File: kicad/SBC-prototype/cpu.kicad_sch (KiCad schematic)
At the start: 5 parts, among them IC2 W65C02S6TPG-14

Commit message: Started including hierarchical flow in the top level sheet
- First, hierarchical designs - I don't need a schematic to all fit on
  one sheet.
- I had the clock and reset lines as global labels, so I converted them
  to hierarchical labels instead, imported them on each sheet, and then
  connected the sheets together. It probably looks like overkill right
  now, but it will allow me to modify each block more easily
- The VIA has unconnected ports for now because I haven't wired them to
  anything on the prototyep in the lab yet. That's next, once the
  EEPROM, SRAM, and address decoders are all working (and VIA1 doesn't
  need a load except for maybe some resistors for now).
- Finally, the power rails and ground are global labels right now and
  aren't connected to anything on the top level design schematic. I'm
  not sure if that's normal, so for now I've just left them.
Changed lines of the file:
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@@
 	(title_block
 		(title "65C02 Single Board Computer")
-		(rev "Mk. 0")
+		(rev "Proto")
 	)
 	(junction
@@
 			(width 0)
 			(type default)
-		)
-	)
-	(global_label "~{RST}"
-		(shape input)
-		(at 54.61 60.96 180)
-		(fields_autoplaced yes)
-		(effects
-			(font
-				(size 1.27 1.27)
-			)
-			(justify right)
-		)
-		(property "Intersheetrefs" "${INTERSHEET_REFS}"
-			(at 48.1777 60.96 0)
-			(effects
-				(font
-					(size 1.27 1.27)
-				)
-				(justify right)
-				(hide yes)
-			)
-		)
-	)
-	(global_label "CLK"
-		(shape input)
-		(at 54.61 85.09 180)
-		(fields_autoplaced yes)
-		(effects
-			(font
-				(size 1.27 1.27)
-			)
-			(justify right)
-		)
-		(property "Intersheetrefs" "${INTERSHEET_REFS}"
-			(at 48.0567 85.09 0)
-			(effects
-				(font
-					(size 1.27 1.27)
-				)
-				(justify right)
-				(hide yes)
-			)
 		)
 	)
@@
 		)
 	)
+	(hierarchical_label "CLK"
+		(shape input)
+		(at 54.61 85.09 180)
+		(fields_autoplaced yes)
+		(effects
+			(font
+				(size 1.27 1.27)
+			)
+			(justify right)
+		)
+	)
 	(hierarchical_label "DATA"
 		(shape bidirectional)
@@
 		)
 	)
+	(hierarchical_label "~{RST}"
+		(shape input)
+		(at 54.61 60.96 180)
+		(fields_autoplaced yes)
+		(effects
+			(font
+				(size 1.27 1.27)
+			)
+			(justify right)
+		)
+	)

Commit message: The pull up resistor for the IRQB and NMIB lines should be 3.3k ohms.
- This might not be accurate - depends on if my interrupt source (the
  65C22) is a n 'S' variant or not, which can pull both up and down.
- That's going to be an inportant detail when it comes to adding other
  VIA because if it pulls both ways, I'll need to AND the interrupt
  sources together instead of wired-OR'ing them.
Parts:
- R3, R4: value 1k -> 3k3
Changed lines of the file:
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@@
 			)
 		)
-		(property "Value" "1k"
+		(property "Value" "3k3"
 			(at 109.22 50.7999 0)
 			(effects
@@
 			)
 		)
-		(property "Value" "1k"
+		(property "Value" "3k3"
 			(at 118.11 50.7999 0)
 			(effects

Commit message: Removed pull up resistor on the IRQB line from VIA 1 to the processor. Confirmed 65C22S with totem pole IRQ.
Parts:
- removed R4: 3k3, symbol Device:R
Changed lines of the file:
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@@
-	)
-	(junction
-		(at 106.68 38.1)
-		(diameter 0)
-		(color 0 0 0 0)
-	)
-	(junction
-		(at 115.57 93.98)
-		(diameter 0)
-		(color 0 0 0 0)
 	)
 	(junction
@@
 	(wire
 		(pts
-			(xy 115.57 93.98) (xy 133.35 93.98)
+			(xy 54.61 93.98) (xy 133.35 93.98)
 		)
 		(stroke
@@
 		)
 	)
-	(wire
-		(pts
-			(xy 54.61 93.98) (xy 115.57 93.98)
-		)
-		(stroke
-			(width 0)
-			(type default)
-		)
-	)
 	(bus
 		(pts
@@
 		)
 	)
-	(wire
-		(pts
-			(xy 115.57 53.34) (xy 115.57 93.98)
-		)
-		(stroke
-			(width 0)
-			(type default)
-		)
-	)
 	(bus
 		(pts
@@
 		)
 	)
-	(wire
-		(pts
-			(xy 115.57 38.1) (xy 115.57 45.72)
-		)
-		(stroke
-			(width 0)
-			(type default)
-		)
-	)
 	(bus
 		(pts
@@
 		(pts
 			(xy 196.85 73.66) (xy 196.85 76.2)
-		)
-		(stroke
-			(width 0)
-			(type default)
-		)
-	)
-	(wire
-		(pts
-			(xy 106.68 38.1) (xy 115.57 38.1)
 		)
 		(stroke
@@
 					(unit 1)
 				)
-			)
-		)
-	)
-	(symbol
-		(lib_id "Device:R")
-		(at 115.57 49.53 0)
-		(unit 1)
-		(exclude_from_sim no)
-		(in_bom yes)
-		(on_board yes)
-		(dnp no)
-		(fields_autoplaced yes)
-		(property "Reference" "R4"
-			(at 118.11 48.2599 0)
-			(effects
-				(font
-					(size 1.27 1.27)
-				)
-				(justify left)
-			)
-		)
-		(property "Value" "3k3"
-			(at 118.11 50.7999 0)
-			(effects
-				(font
-					(size 1.27 1.27)
-				)
-				(justify left)
-			)
-		)
-		(property "Footprint" ""
-			(at 113.792 49.53 90)
-			(effects
-				(font
-					(size 1.27 1.27)
-				)
-				(hide yes)
-			)
-		)
-		(property "Datasheet" "~"
-			(at 115.57 49.53 0)
-			(effects
-				(font
-					(size 1.27 1.27)
-				)
-				(hide yes)
-			)
-		)
-		(property "Description" "Resistor"
-			(at 115.57 49.53 0)
-			(effects
-				(font
-					(size 1.27 1.27)
-				)
-				(hide yes)
-			)
-		)
-		(pin "1"
-		)
-		(pin "2"
-		)
-		(instances
-			(project "SBC-prototype"
-				(path "/1c8fb460-190a-4823-a6aa-9b1d397d6158/0456201c-b4b8-4a85-8590-2dcf9ac729a4"
-					(reference "R4")
-					(unit 1)
-				)

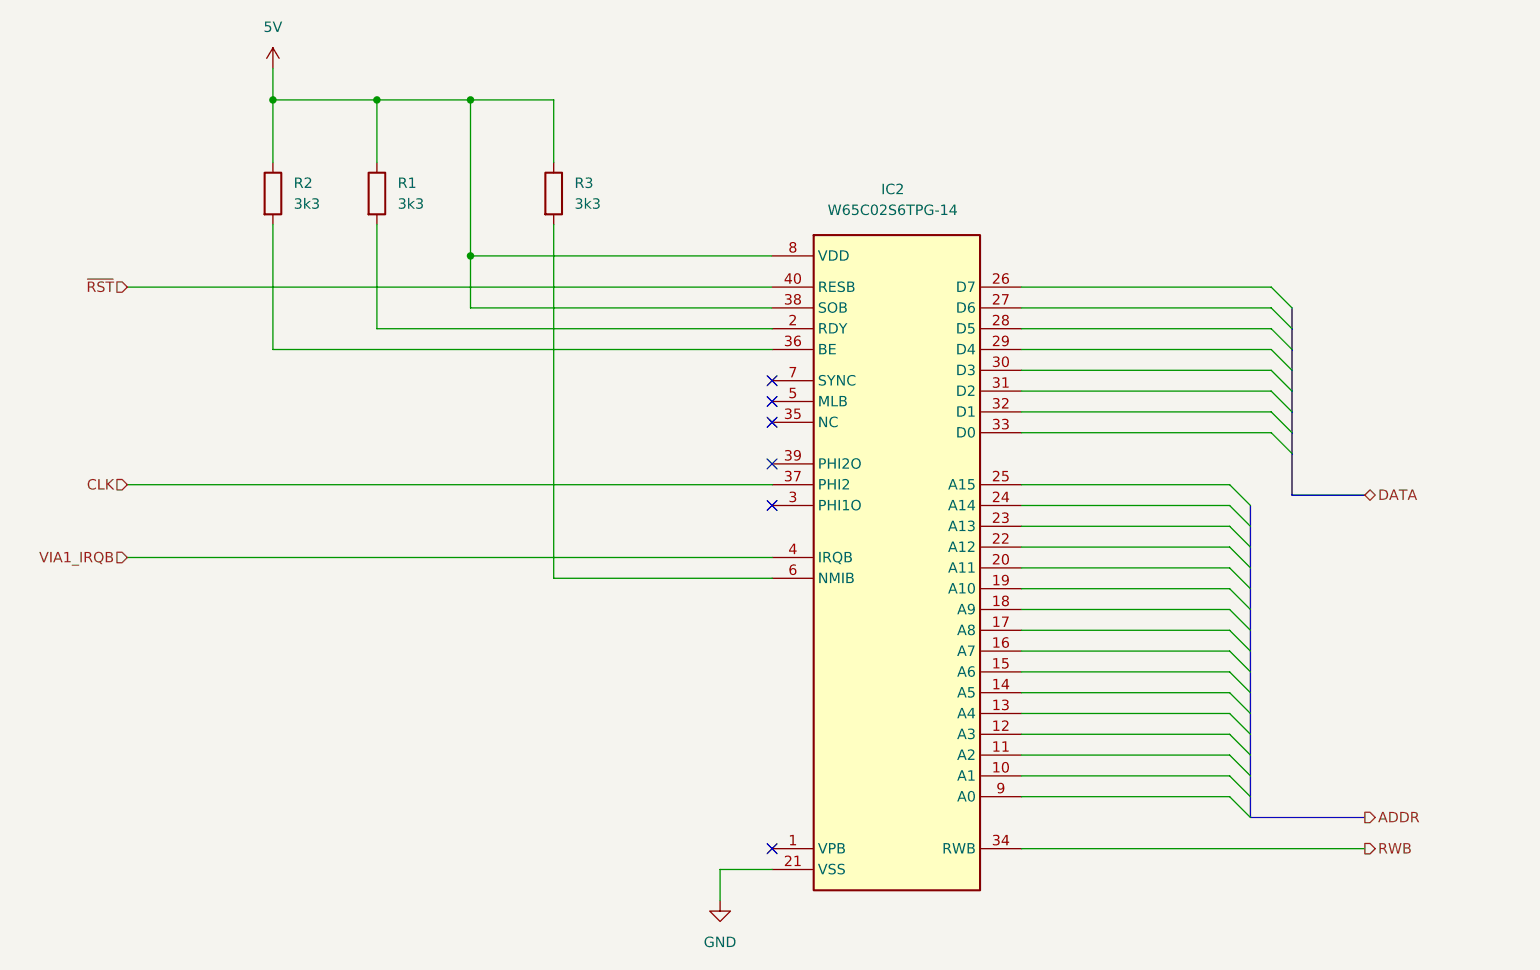
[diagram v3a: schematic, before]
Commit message: Fixed a ton of DRC errors and warnings
- VIA 1 is still unconnected since it's on the breadboard that way and I
  haven't hooked it to anything yet
- All the parts in the library have changed because I've modified my own
  versions of them. I'm not sure if I should add my changes to the
  library or find a way to tell the tool that it's OK that those are
  updated.
- The 74HC00 NAND gate was completely broken and would have been an
  interesting problem to sort out during routing and placement
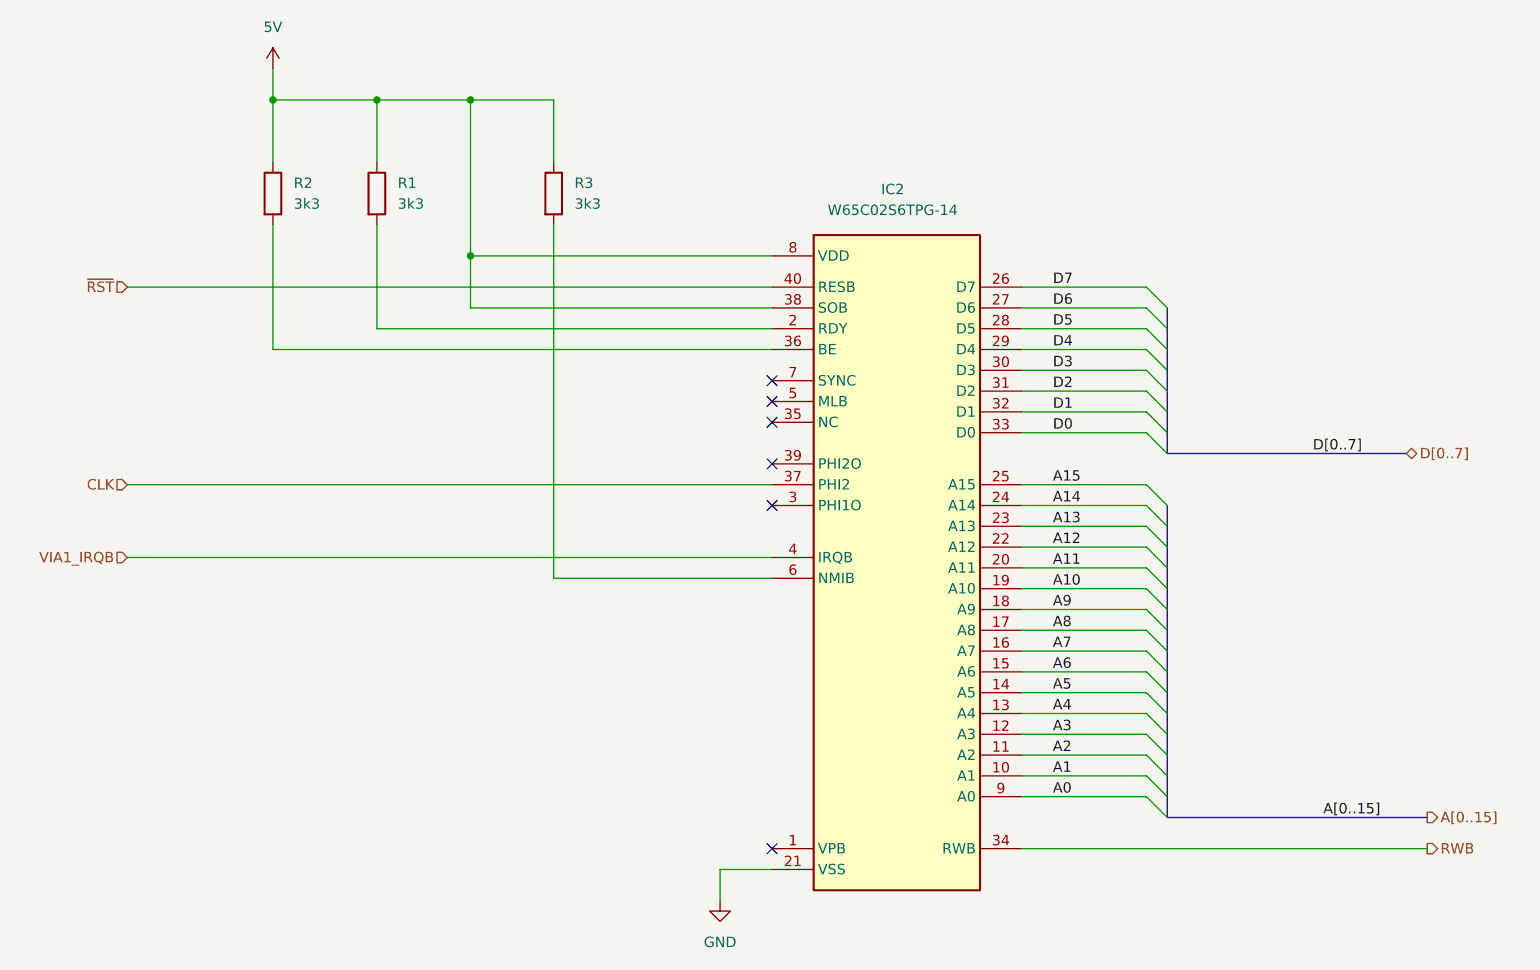
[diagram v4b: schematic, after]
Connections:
- net A1: now reaches IC2.10 (A1)
- net A2: now reaches IC2.11 (A2)
- net A3: now reaches IC2.12 (A3)
- net A4: now reaches IC2.13 (A4)
- net A5: now reaches IC2.14 (A5)
- net A6: now reaches IC2.15 (A6)
- net A7: now reaches IC2.16 (A7)
- net A8: now reaches IC2.17 (A8)
- net A9: now reaches IC2.18 (A9)
- net A10: now reaches IC2.19 (A10)
- net A11: now reaches IC2.20 (A11)
- net A12: now reaches IC2.22 (A12)
- net A13: now reaches IC2.23 (A13)
- net A14: now reaches IC2.24 (A14)
- net A15: now reaches IC2.25 (A15)
- net D7: now reaches IC2.26 (D7)
- net D6: now reaches IC2.27 (D6)
- net D5: now reaches IC2.28 (D5)
- net D4: now reaches IC2.29 (D4)
- net D3: now reaches IC2.30 (D3)
- net D2: now reaches IC2.31 (D2)
- net D1: now reaches IC2.32 (D1)
- net D0: now reaches IC2.33 (D0)
- net A0: now reaches IC2.9 (A0)
